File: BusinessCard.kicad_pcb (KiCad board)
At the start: 2 copper layers, 88.9 x 50.8 mm, 7 parts, among them Q1 Q_NMOS_DGS

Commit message: First draft of front
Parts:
- added BT1: Battery_Cell, CardElements:Linx_CR2032_Holder, F.Cu at (68.6, 75.7)
- added P1: ButtonPad, CardElements:ButtonPad, F.Cu at (99.1, 96.8)
- added P2: ButtonPad, CardElements:ButtonPad, F.Cu at (99.1, 90.2)
- added P3: ButtonPad, CardElements:ButtonPad, F.Cu at (126.0, 96.8)
- added P4: ButtonPad, CardElements:ButtonPad, F.Cu at (126.0, 90.2)
- added svg2mod: G***, CardElements:front, F.Cu at (92.7, 72.4)
- moved Q1 10.9 mm to (78.0, 92.5)
- moved D5 3.44 mm to (54.3, 67.9)
- moved D1 2.94 mm to (54.3, 84.5)
- moved D4 2.84 mm to (68.6, 59.7)
- moved D2 2.71 mm to (68.6, 92.7)
- moved D6 1.93 mm to (82.9, 67.9)
- moved D3 0.72 mm to (82.9, 84.5)
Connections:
- net Net-(BT1-Pad1) renamed +3V3
- net Net-(D1-Pad1) renamed Cathode
- Q1 pad 2: Net-(Q1-Pad2) -> Sense
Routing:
- net Sense: track 0.00 -> 52.6 mm
- net +3V3: track 0.00 -> 2.54 mm, vias 0 -> 1
- removed copper zone on F.Cu, net GND
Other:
- net class Default: clearance 0.2 -> 0.254; trace_width 0.25 -> 0.508; via_dia 0.6 -> 0.6858; via_drill 0.4 -> 0.3048
- rule trace_clearance: 0.2 -> 0.254
- board text removed: "Maker & Electrical Engineer"
- board text removed: "OFF"
- board text removed: "ON"
- board text removed: "Sunny He"

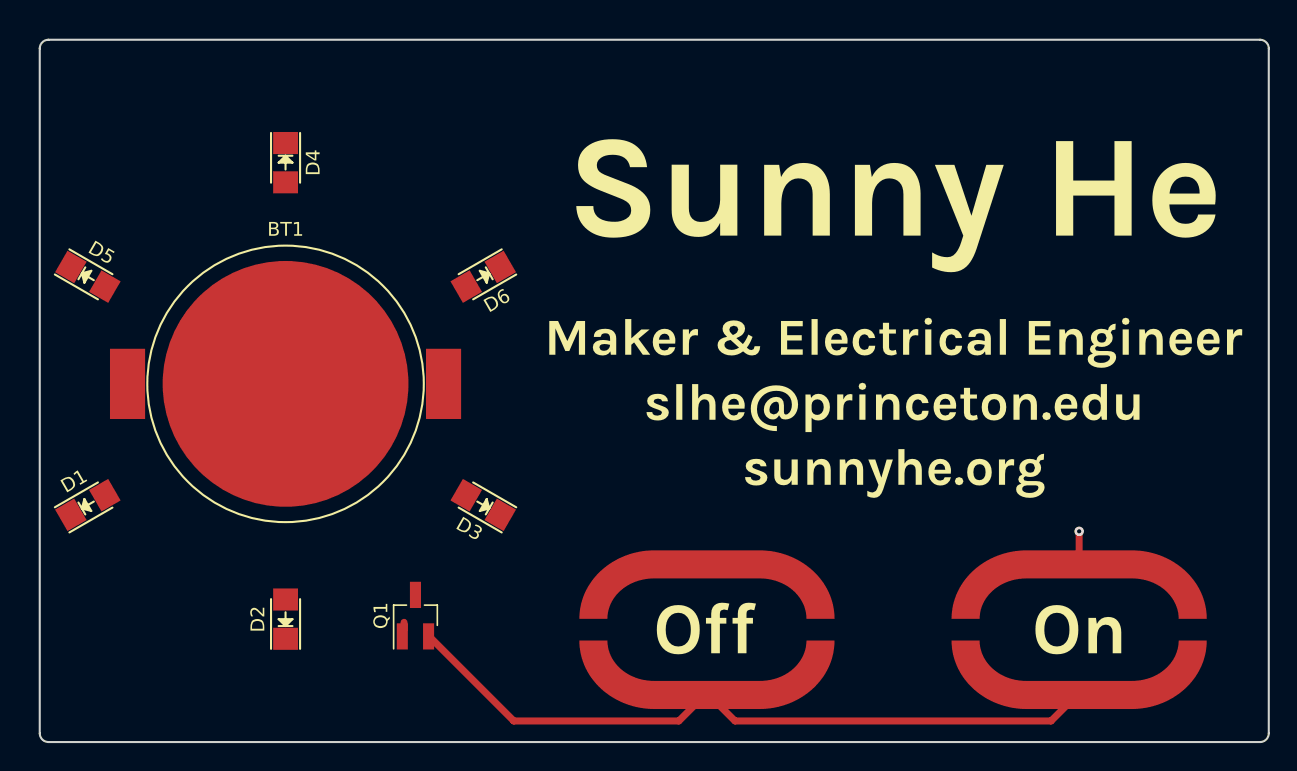
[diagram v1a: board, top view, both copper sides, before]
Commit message: Front placement complete
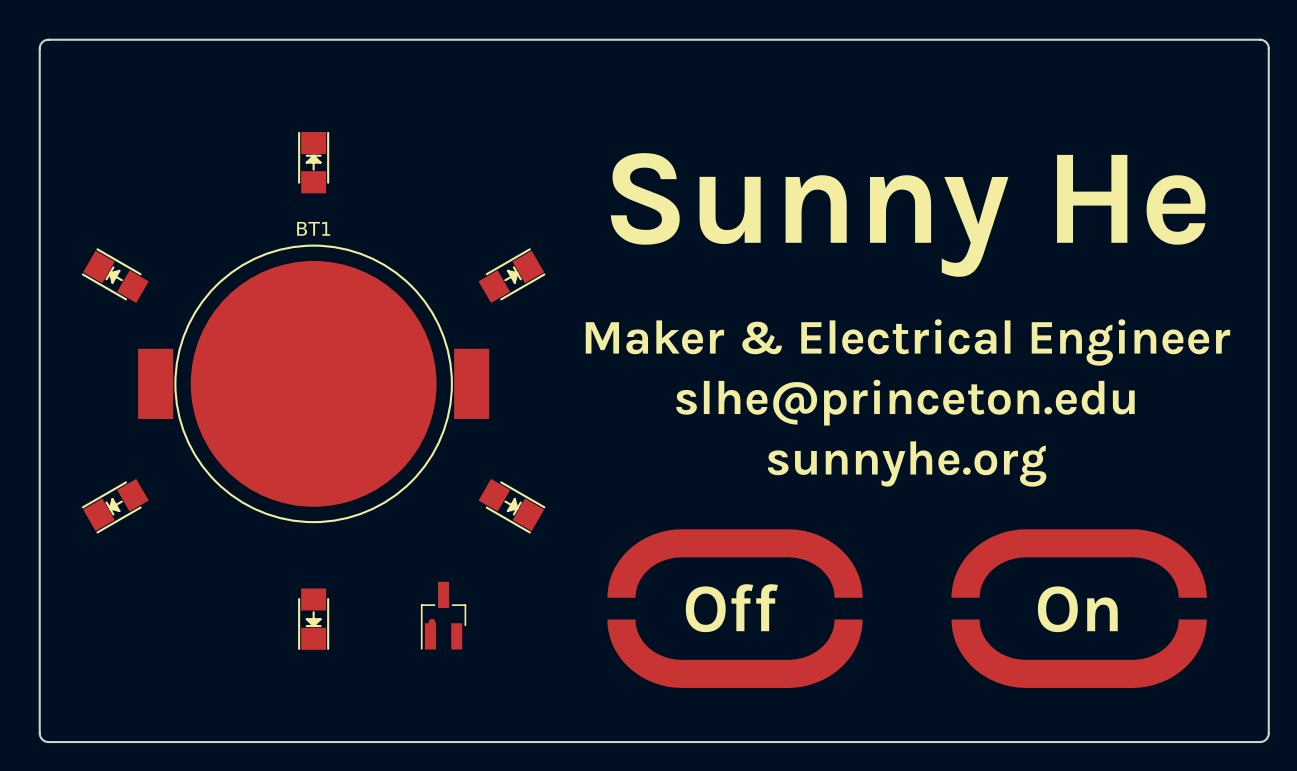
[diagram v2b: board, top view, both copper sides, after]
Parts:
- moved P1 2.54 mm to (101.1, 95.2)
- moved P2 2.54 mm to (101.1, 88.6)
- moved svg2mod 2.29 mm to (95.0, 72.4)
- moved Q1 2.03 mm to (80.0, 92.5)
- moved BT1 2.03 mm to (70.6, 75.7)
- moved D1 2.03 mm to (56.3, 84.5)
- moved D2 2.03 mm to (70.6, 92.7)
- moved D3 2.03 mm to (84.9, 84.5)
- moved D4 2.03 mm to (70.6, 59.7)
- moved D5 2.03 mm to (56.3, 67.9)
- moved D6 2.03 mm to (84.9, 67.9)
- moved P3 1.52 mm to (126.0, 95.2)
- moved P4 1.52 mm to (126.0, 88.6)
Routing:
- net Sense: track 52.6 -> 0.00 mm
- net +3V3: track 2.54 -> 0.00 mm, vias 1 -> 0
- net Cathode: track 0.00 -> 0.55 mm

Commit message: Preliminary routing
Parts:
- moved Q1 0.19 mm to (80.2, 92.5)
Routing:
- net +3V3: track 0.00 -> 139.0 mm, vias 0 -> 2
- net Cathode: track 0.55 -> 117.2 mm, vias 0 -> 7
- net Sense: track 0.00 -> 49.5 mm
- net GND: track 0.00 -> 2.03 mm, vias 0 -> 1
- added copper zone on B.Cu, net GND
- added copper zone on F.Cu, net GND
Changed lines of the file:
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@@
     (links 18)
     (no_connects 17)
-    (area 50.724999 50.724999 140.791001 101.675001)
+    (area 50.724999 50.724999 139.775001 101.675001)
     (thickness 1.6)
     (drawings 10)
-    (tracks 1)
+    (tracks 46)
     (zones 0)
     (modules 13)
@@
   )
   (module TO_SOT_Packages_SMD:SOT-23_Handsoldering (layer F.Cu)
-    (at 80.01 92.456 90)
+    (at 80.198 92.48 90)
     (descr "SOT-23, Handsoldering")
     (tags SOT-23)
@@
   (gr_line (start 139.7 51.435) (end 139.7 100.965) (layer Edge.Cuts) (width 0.15))
   (gr_line (start 51.435 50.8) (end 139.065 50.8) (layer Edge.Cuts) (width 0.15))
-  (segment (start 79.182 93.49) (end 79.182 92.94) (width 0.508) (layer F.Cu) (net 3))
+  (segment (start 101.092 87.376) (end 101.092 85.344) (width 0.508) (layer F.Cu) (net 1))
+  (via (at 101.092 85.344) (size 0.6858) (drill 0.3048) (layers F.Cu B.Cu) (net 1))
+  (segment (start 81.28 82.296) (end 81.788 81.788) (width 0.508) (layer B.Cu) (net 2))
+  (segment (start 81.788 81.788) (end 122.428 81.788) (width 0.508) (layer B.Cu) (net 2))
+  (segment (start 122.428 81.788) (end 125.984 85.344) (width 0.508) (layer B.Cu) (net 2))
+  (segment (start 125.984 85.344) (end 125.984 87.376) (width 0.508) (layer F.Cu) (net 2))
+  (via (at 125.984 85.344) (size 0.6858) (drill 0.3048) (layers F.Cu B.Cu) (net 2))
+  (segment (start 81.330646 82.296) (end 83.682565 83.74507) (width 0.508) (layer F.Cu) (net 2))
+  (segment (start 70.612 75.692) (end 81.330646 82.296) (width 0.508) (layer F.Cu) (net 2))
+  (via (at 81.330646 82.296) (size 0.6858) (drill 0.3048) (layers F.Cu B.Cu) (net 2))
+  (segment (start 57.541435 83.74507) (end 70.612 75.692) (width 0.508) (layer F.Cu) (net 2))
+  (segment (start 57.541435 68.65493) (end 70.612 75.692) (width 0.508) (layer F.Cu) (net 2))
+  (segment (start 70.612 61.10986) (end 70.612 75.692) (width 0.508) (layer F.Cu) (net 2))
+  (segment (start 83.682565 68.65493) (end 70.612 75.692) (width 0.508) (layer F.Cu) (net 2))
+  (segment (start 70.612 91.29014) (end 70.612 75.692) (width 0.508) (layer F.Cu) (net 2))
+  (segment (start 79.248 96.012) (end 79.248 93.98) (width 0.508) (layer F.Cu) (net 3))
+  (segment (start 87.884 89.916) (end 81.788 96.012) (width 0.508) (layer B.Cu) (net 3))
+  (segment (start 81.788 96.012) (end 79.248 96.012) (width 0.508) (layer B.Cu) (net 3))
+  (via (at 79.248 96.012) (size 0.6858) (drill 0.3048) (layers F.Cu B.Cu) (net 3))
+  (segment (start 87.884 86.106) (end 87.884 89.916) (width 0.508) (layer B.Cu) (net 3))
+  (segment (start 79.06 93.956) (end 79.036 93.98) (width 0.508) (layer F.Cu) (net 3))
+  (segment (start 79.036 93.98) (end 70.76186 93.98) (width 0.508) (layer F.Cu) (net 3))
+  (segment (start 70.76186 93.98) (end 70.612 94.12986) (width 0.508) (layer F.Cu) (net 3))
+  (segment (start 88.138 66.167) (end 70.612 56.388) (width 0.508) (layer B.Cu) (net 3))
+  (segment (start 86.141835 67.23507) (end 88.138 66.167) (width 0.508) (layer F.Cu) (net 3))
+  (via (at 88.138 66.167) (size 0.6858) (drill 0.3048) (layers F.Cu B.Cu) (net 3))
+  (segment (start 70.612 56.388) (end 53.34 66.294) (width 0.508) (layer B.Cu) (net 3))
+  (via (at 70.612 56.388) (size 0.6858) (drill 0.3048) (layers F.Cu B.Cu) (net 3))
+  (segment (start 70.612 58.27014) (end 70.612 56.388) (width 0.508) (layer F.Cu) (net 3))
+  (segment (start 86.141835 85.16493) (end 87.884 86.106) (width 0.508) (layer F.Cu) (net 3))
+  (via (at 87.884 86.106) (size 0.6858) (drill 0.3048) (layers F.Cu B.Cu) (net 3))
+  (segment (start 53.34 86.106) (end 55.082165 85.16493) (width 0.508) (layer F.Cu) (net 3))
+  (segment (start 53.34 66.294) (end 55.082165 67.23507) (width 0.508) (layer F.Cu) (net 3))
+  (segment (start 53.34 86.106) (end 53.34 66.294) (width 0.508) (layer B.Cu) (net 3))
+  (via (at 53.34 66.294) (size 0.6858) (drill 0.3048) (layers F.Cu B.Cu) (net 3))
+  (segment (start 53.34 86.106) (end 70.612 96.012) (width 0.508) (layer B.Cu) (net 3))
+  (via (at 53.34 86.106) (size 0.6858) (drill 0.3048) (layers F.Cu B.Cu) (net 3))
+  (segment (start 70.612 94.12986) (end 70.612 96.012) (width 0.508) (layer F.Cu) (net 3))
+  (via (at 70.612 96.012) (size 0.6858) (drill 0.3048) (layers F.Cu B.Cu) (net 3))
+  (segment (start 85.344 98.552) (end 99.06 98.552) (width 0.508) (layer F.Cu) (net 4))
+  (segment (start 85.344 98.552) (end 81.148 94.356) (width 0.508) (layer F.Cu) (net 4))
+  (segment (start 81.148 94.356) (end 81.148 93.98) (width 0.508) (layer F.Cu) (net 4))
+  (segment (start 101.092 96.52) (end 99.06 98.552) (width 0.508) (layer F.Cu) (net 4))
+  (segment (start 125.984 96.52) (end 123.952 98.552) (width 0.508) (layer F.Cu) (net 4))
+  (segment (start 103.124 98.552) (end 101.092 96.52) (width 0.508) (layer F.Cu) (net 4))
+  (segment (start 123.952 98.552) (end 103.124 98.552) (width 0.508) (layer F.Cu) (net 4))
+  (zone (net 1) (net_name GND) (layer F.Cu) (hatch edge 0.508)
+    (connect_pads (clearance 0.508))
+    (min_thickness 0.254)
+    (fill yes (arc_segments 16) (thermal_gap 0.508) (thermal_bridge_width 0.508))
+    (polygon
+      (pts
+        (xy 51.435 51.435) (xy 51.435 100.965) (xy 139.065 100.965) (xy 139.065 51.435)
+      )
+    )
+  )
+  (zone (net 1) (net_name GND) (layer B.Cu) (hatch edge 0.508)
+    (connect_pads (clearance 0.508))
+    (min_thickness 0.254)
+    (fill yes (arc_segments 16) (thermal_gap 0.508) (thermal_bridge_width 0.508))
+    (polygon
+      (pts
+        (xy 51.435 51.435) (xy 51.435 100.965) (xy 139.065 100.965) (xy 139.065 51.435)
+      )
+    )
+  )
 )

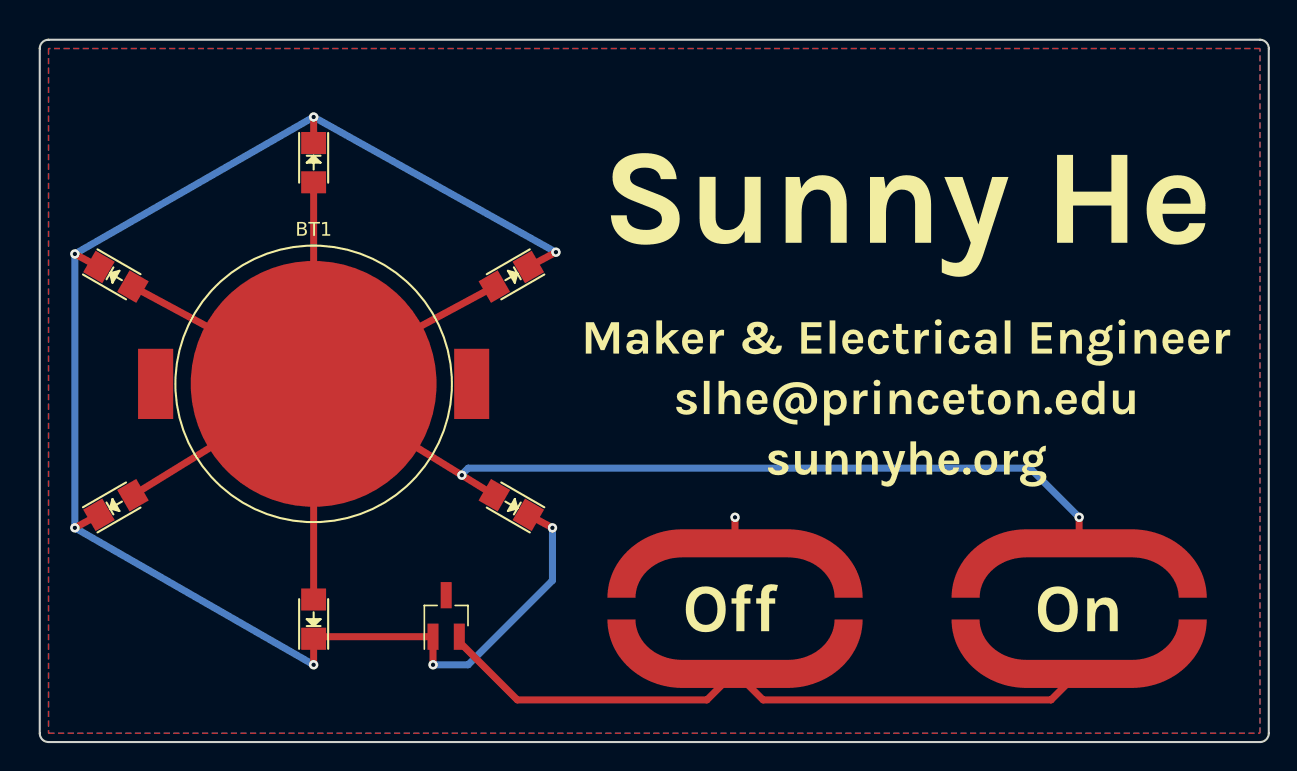
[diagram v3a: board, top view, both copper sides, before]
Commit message: Finish stitching, fixed pad assignments
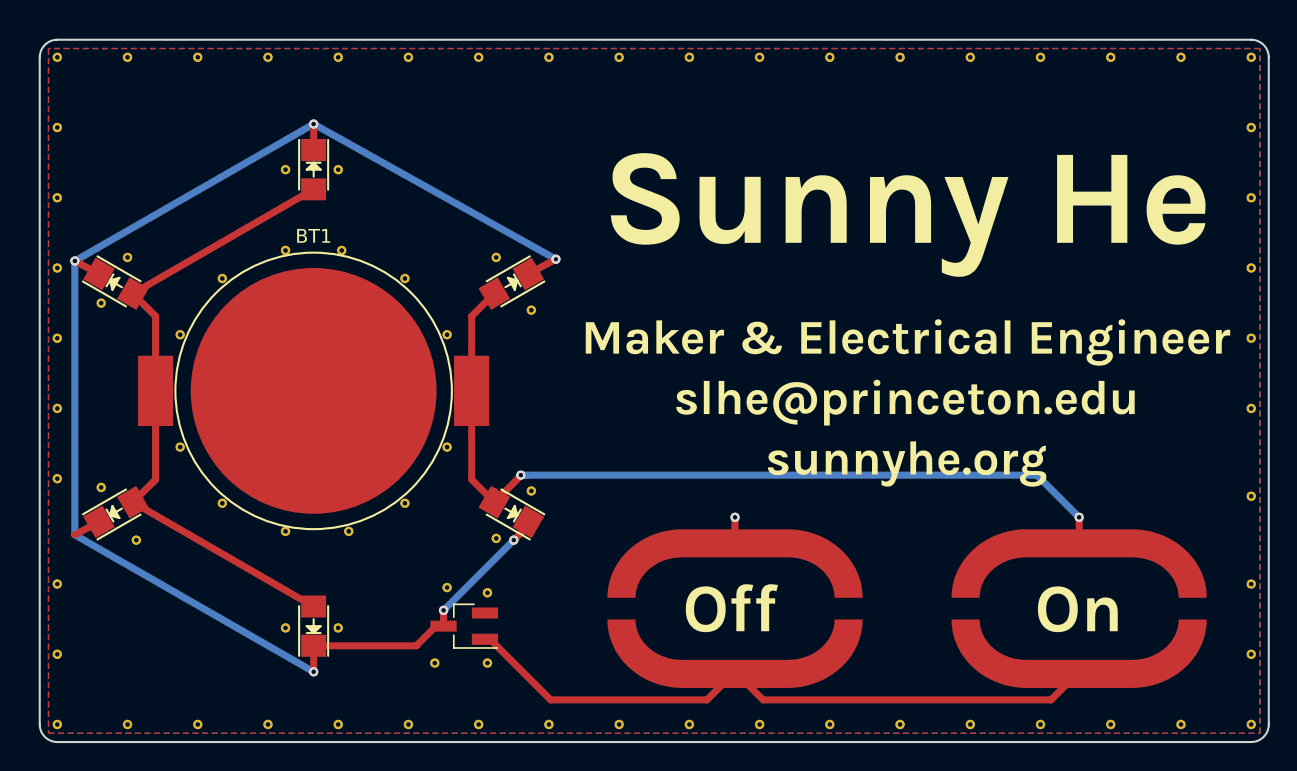
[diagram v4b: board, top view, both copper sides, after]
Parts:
- added REF**: VIA_13_7, Vias:VIA_13_7, F.Cu at (80.3, 90.4)
- added REF**: VIA_13_7, Vias:VIA_13_7, F.Cu at (61.0, 72.1)
- added REF**: VIA_13_7, Vias:VIA_13_7, F.Cu at (64.0, 68.1)
- added REF**: VIA_13_7, Vias:VIA_13_7, F.Cu at (72.6, 66.0)
- added REF**: VIA_13_7, Vias:VIA_13_7, F.Cu at (68.6, 66.0)
- added REF**: VIA_13_7, Vias:VIA_13_7, F.Cu at (79.4, 95.9)
- added REF**: VIA_13_7, Vias:VIA_13_7, F.Cu at (83.2, 95.9)
- added REF**: VIA_13_7, Vias:VIA_13_7, F.Cu at (72.4, 93.3)
- added REF**: VIA_13_7, Vias:VIA_13_7, F.Cu at (68.6, 93.3)
- added REF**: VIA_13_7, Vias:VIA_13_7, F.Cu at (57.8, 87.0)
- added REF**: VIA_13_7, Vias:VIA_13_7, F.Cu at (55.2, 83.2)
- added REF**: VIA_13_7, Vias:VIA_13_7, F.Cu at (80.3, 80.3)
- added REF**: VIA_13_7, Vias:VIA_13_7, F.Cu at (55.2, 69.8)
- added REF**: VIA_13_7, Vias:VIA_13_7, F.Cu at (83.2, 90.8)
- added REF**: VIA_13_7, Vias:VIA_13_7, F.Cu at (83.8, 86.9)
- added REF**: VIA_13_7, Vias:VIA_13_7, F.Cu at (86.4, 83.4)
- added REF**: VIA_13_7, Vias:VIA_13_7, F.Cu at (86.4, 70.4)
- added REF**: VIA_13_7, Vias:VIA_13_7, F.Cu at (83.8, 66.5)
- added REF**: VIA_13_7, Vias:VIA_13_7, F.Cu at (72.4, 60.2)
- added REF**: VIA_13_7, Vias:VIA_13_7, F.Cu at (68.6, 60.2)
- added REF**: VIA_13_7, Vias:VIA_13_7, F.Cu at (57.1, 66.5)
- added REF**: VIA_13_7, Vias:VIA_13_7, F.Cu at (92.7, 52.1)
- added REF**: VIA_13_7, Vias:VIA_13_7, F.Cu at (80.3, 72.1)
- added REF**: VIA_13_7, Vias:VIA_13_7, F.Cu at (97.8, 52.1)
- added REF**: VIA_13_7, Vias:VIA_13_7, F.Cu at (123.2, 52.1)
- added REF**: VIA_13_7, Vias:VIA_13_7, F.Cu at (133.3, 52.1)
- added REF**: VIA_13_7, Vias:VIA_13_7, F.Cu at (128.3, 52.1)
- added REF**: VIA_13_7, Vias:VIA_13_7, F.Cu at (113.0, 52.1)
- added REF**: VIA_13_7, Vias:VIA_13_7, F.Cu at (108.0, 52.1)
- added REF**: VIA_13_7, Vias:VIA_13_7, F.Cu at (102.9, 52.1)
- added REF**: VIA_13_7, Vias:VIA_13_7, F.Cu at (118.1, 52.1)
- added REF**: VIA_13_7, Vias:VIA_13_7, F.Cu at (57.1, 52.1)
- added REF**: VIA_13_7, Vias:VIA_13_7, F.Cu at (67.3, 52.1)
- added REF**: VIA_13_7, Vias:VIA_13_7, F.Cu at (77.2, 68.1)
- added REF**: VIA_13_7, Vias:VIA_13_7, F.Cu at (62.2, 52.1)
- added REF**: VIA_13_7, Vias:VIA_13_7, F.Cu at (87.6, 52.1)
- added REF**: VIA_13_7, Vias:VIA_13_7, F.Cu at (72.4, 52.1)
- added REF**: VIA_13_7, Vias:VIA_13_7, F.Cu at (82.5, 52.1)
- added REF**: VIA_13_7, Vias:VIA_13_7, F.Cu at (77.5, 52.1)
- added REF**: VIA_13_7, Vias:VIA_13_7, F.Cu at (133.3, 100.3)
- added REF**: VIA_13_7, Vias:VIA_13_7, F.Cu at (128.3, 100.3)
- added REF**: VIA_13_7, Vias:VIA_13_7, F.Cu at (123.2, 100.3)
- added REF**: VIA_13_7, Vias:VIA_13_7, F.Cu at (118.1, 100.3)
- added REF**: VIA_13_7, Vias:VIA_13_7, F.Cu at (113.0, 100.3)
- added REF**: VIA_13_7, Vias:VIA_13_7, F.Cu at (77.2, 84.3)
- added REF**: VIA_13_7, Vias:VIA_13_7, F.Cu at (108.0, 100.3)
- added REF**: VIA_13_7, Vias:VIA_13_7, F.Cu at (102.9, 100.3)
- added REF**: VIA_13_7, Vias:VIA_13_7, F.Cu at (97.8, 100.3)
- added REF**: VIA_13_7, Vias:VIA_13_7, F.Cu at (92.7, 100.3)
- added REF**: VIA_13_7, Vias:VIA_13_7, F.Cu at (87.6, 100.3)
- added REF**: VIA_13_7, Vias:VIA_13_7, F.Cu at (82.5, 100.3)
- added REF**: VIA_13_7, Vias:VIA_13_7, F.Cu at (77.5, 100.3)
- added REF**: VIA_13_7, Vias:VIA_13_7, F.Cu at (72.4, 100.3)
- added REF**: VIA_13_7, Vias:VIA_13_7, F.Cu at (67.3, 100.3)
- added REF**: VIA_13_7, Vias:VIA_13_7, F.Cu at (62.2, 100.3)
- added REF**: VIA_13_7, Vias:VIA_13_7, F.Cu at (73.2, 86.4)
- added REF**: VIA_13_7, Vias:VIA_13_7, F.Cu at (57.1, 100.3)
- added REF**: VIA_13_7, Vias:VIA_13_7, F.Cu at (138.4, 57.1)
- added REF**: VIA_13_7, Vias:VIA_13_7, F.Cu at (138.4, 52.1)
- added REF**: VIA_13_7, Vias:VIA_13_7, F.Cu at (138.4, 72.4)
- added REF**: VIA_13_7, Vias:VIA_13_7, F.Cu at (138.4, 67.3)
- added REF**: VIA_13_7, Vias:VIA_13_7, F.Cu at (138.4, 62.2)
- added REF**: VIA_13_7, Vias:VIA_13_7, F.Cu at (138.4, 100.3)
- added REF**: VIA_13_7, Vias:VIA_13_7, F.Cu at (138.4, 90.2)
- added REF**: VIA_13_7, Vias:VIA_13_7, F.Cu at (138.4, 83.8)
- added REF**: VIA_13_7, Vias:VIA_13_7, F.Cu at (138.4, 95.2)
- added REF**: VIA_13_7, Vias:VIA_13_7, F.Cu at (68.6, 86.4)
- added REF**: VIA_13_7, Vias:VIA_13_7, F.Cu at (138.4, 77.5)
- added REF**: VIA_13_7, Vias:VIA_13_7, F.Cu at (52.1, 100.3)
- added REF**: VIA_13_7, Vias:VIA_13_7, F.Cu at (52.1, 95.2)
- added REF**: VIA_13_7, Vias:VIA_13_7, F.Cu at (52.1, 90.2)
- added REF**: VIA_13_7, Vias:VIA_13_7, F.Cu at (52.1, 82.5)
- added REF**: VIA_13_7, Vias:VIA_13_7, F.Cu at (52.1, 77.5)
- added REF**: VIA_13_7, Vias:VIA_13_7, F.Cu at (52.1, 72.4)
- added REF**: VIA_13_7, Vias:VIA_13_7, F.Cu at (52.1, 67.3)
- added REF**: VIA_13_7, Vias:VIA_13_7, F.Cu at (52.1, 62.2)
- added REF**: VIA_13_7, Vias:VIA_13_7, F.Cu at (52.1, 57.1)
- added REF**: VIA_13_7, Vias:VIA_13_7, F.Cu at (64.0, 84.3)
- added REF**: VIA_13_7, Vias:VIA_13_7, F.Cu at (52.1, 52.1)
- added REF**: VIA_13_7, Vias:VIA_13_7, F.Cu at (61.0, 80.3)
- BT1: footprint CardElements:Linx_CR2032_Holder -> Linx_CR2032_Holder
- Q1: footprint TO_SOT_Packages_SMD:SOT-23_Handsoldering -> CardElements:SOT-23_Handsoldering_DGS
- moved Q1 1.51 mm to (81.5, 93.2), turned to 180 degrees
- moved BT1 0.51 mm to (70.6, 76.2)
- moved D2 0.51 mm to (70.6, 93.2)
- moved D5 0.51 mm to (56.3, 68.5)
- moved D6 0.51 mm to (84.9, 68.5)
- moved D4 0.51 mm to (70.6, 60.2)
- moved D1 0.51 mm to (56.3, 85.0)
- moved D3 0.51 mm to (84.9, 85.0)
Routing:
- net +3V3: track 139.0 -> 110.6 mm
- net Cathode: track 117.2 -> 110.0 mm, vias 7 -> 6
- net Sense: track 49.5 -> 47.3 mm
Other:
- outline, holes or cut-outs redrawn
- net class Default: via_drill 0.3048 -> 0.3302
